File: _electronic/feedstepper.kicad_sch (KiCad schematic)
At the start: 11 parts

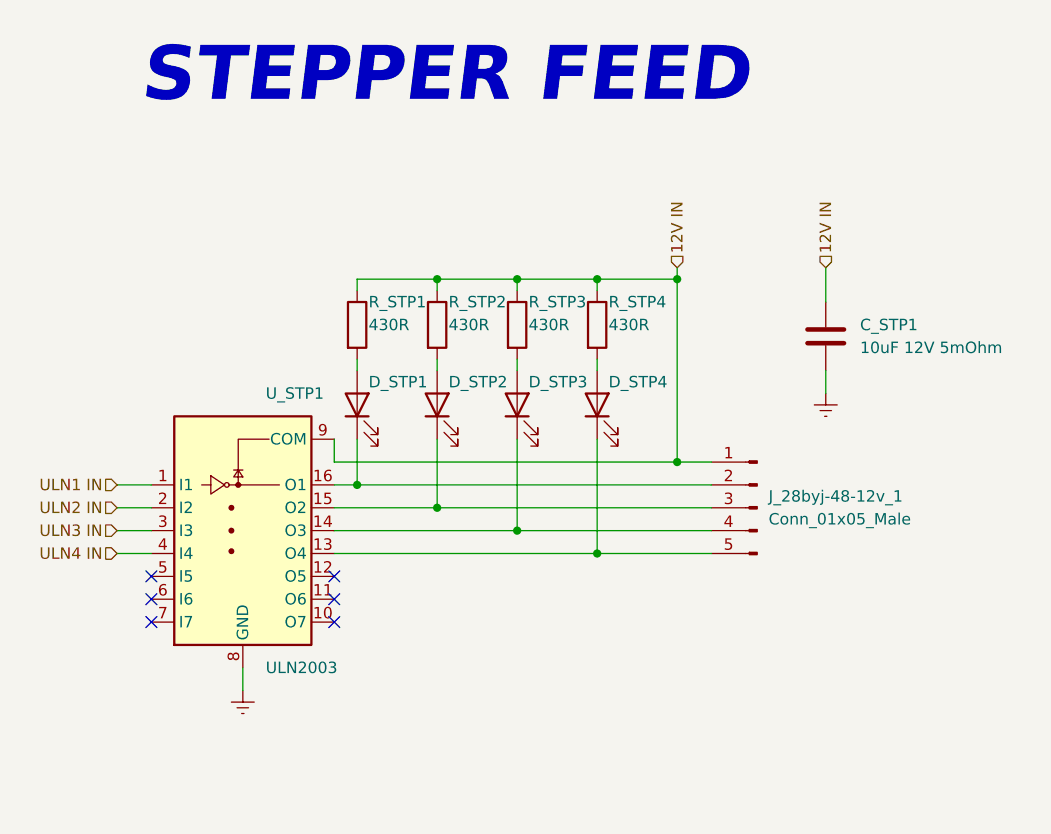
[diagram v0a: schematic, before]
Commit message: led resistor revision, b.o.m. and pcb anotation
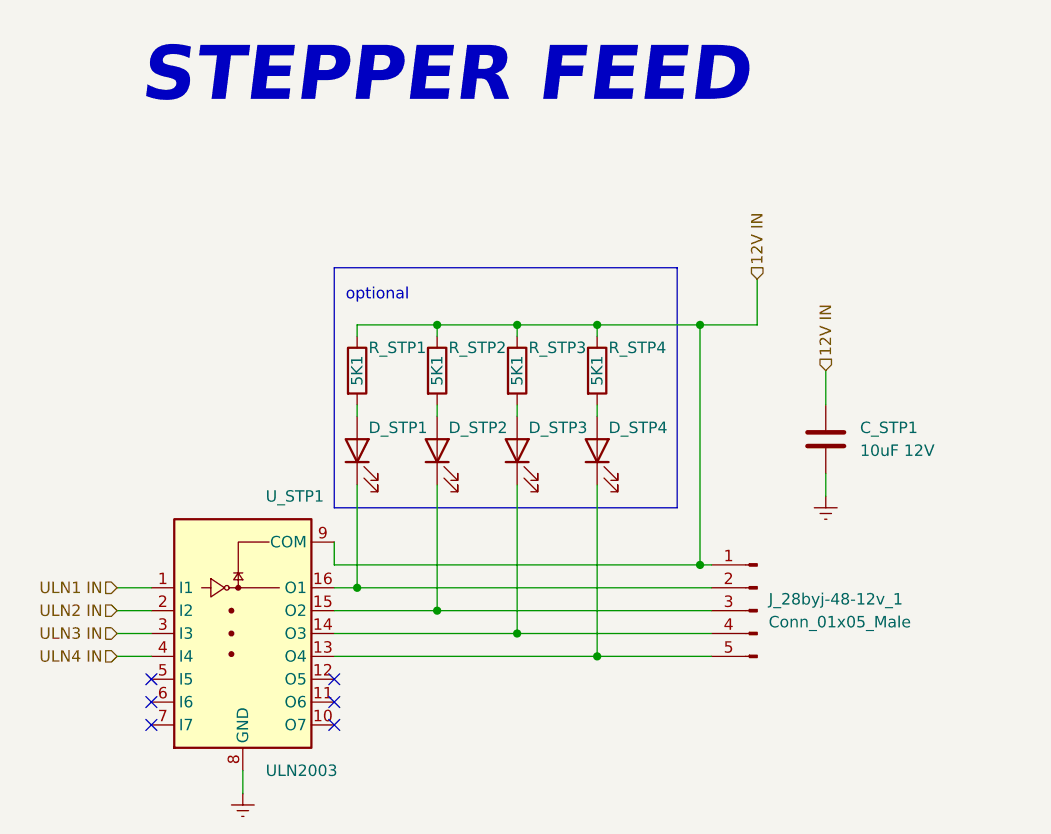
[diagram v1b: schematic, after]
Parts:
- C_STP1: value 10uF 12V 5mOhm -> 10uF 12V; # C1608X5R1E106M080AC -> GRM188Z71A106KA73D
- R_STP1, R_STP2, R_STP3, R_STP4: value 430R -> 5K1; # CR0603-JW-431ELF -> ERJ-3EKF5101V
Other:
- note added: "optional"
- moved on the sheet: C_STP1, D_STP1, D_STP2, D_STP3, D_STP4, J_28byj-48-12v_1, R_STP1, R_STP2, R_STP3, R_STP4, U_STP1

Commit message: schematics and pcb cleanup
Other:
- note added: "optional LED feedback"
- note removed: "optional"
- title: E-TKT -> E-TKT v1.0
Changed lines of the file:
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@@
   (paper "A4")
   (title_block
-    (title "E-TKT")
-    (date "2022-07-21")
-    (rev "3")
+    (title "E-TKT v1.0")
+    (date "2022-09-29")
+    (rev "4")
     (company "Andrei Speridiao")
   )
@@
     (stroke (width 0) (type default) (color 0 0 0 0))
   )
-  (text "optional" (at 134.62 87.63 0)
+  (text "optional LED feedback" (at 134.62 87.63 0)
     (effects (font (size 1.27 1.27)) (justify left bottom))
   )
